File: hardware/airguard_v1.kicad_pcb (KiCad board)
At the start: 2 copper layers, 2 parts, among them U1 MH-Z19B, U2 ESP32_DEVKIT_C

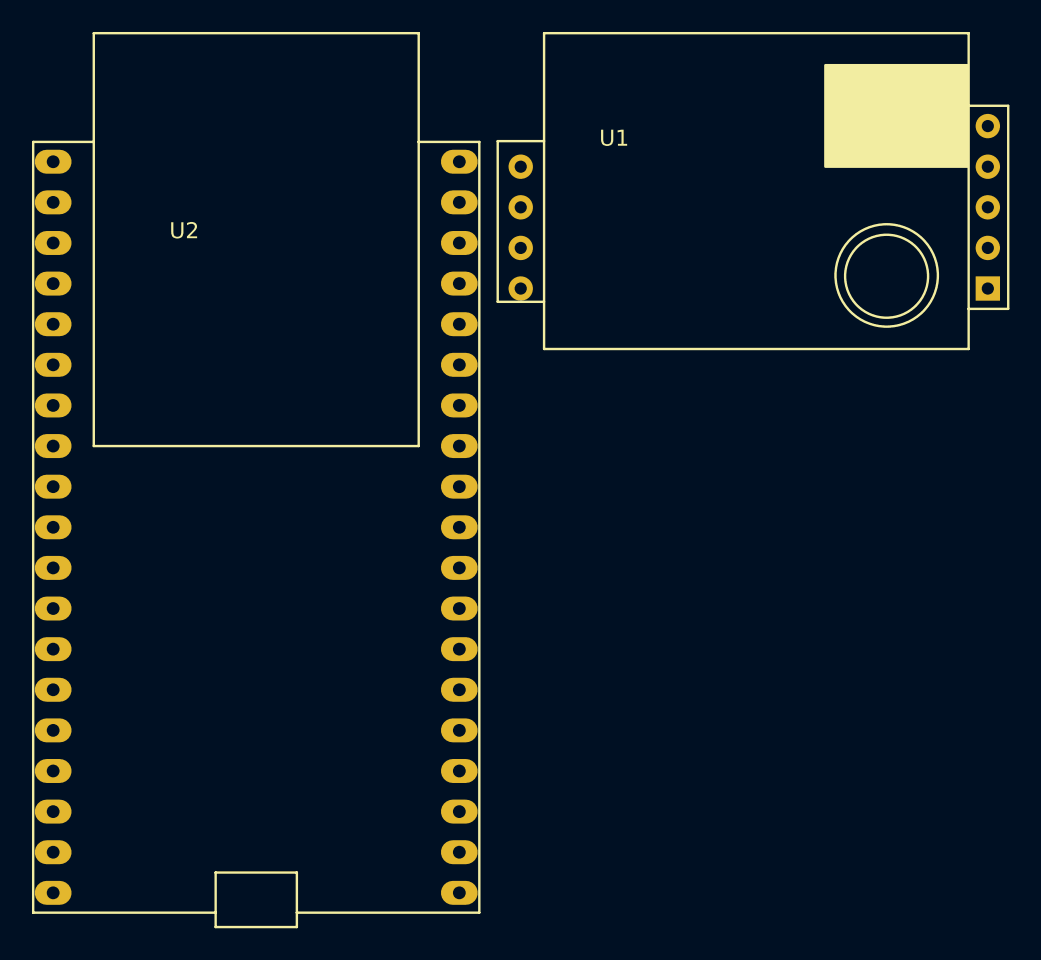
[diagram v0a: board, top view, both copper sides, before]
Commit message: Adding the OLED and all 3d models; connecting some of the signals to the corresponding ESP32 pins
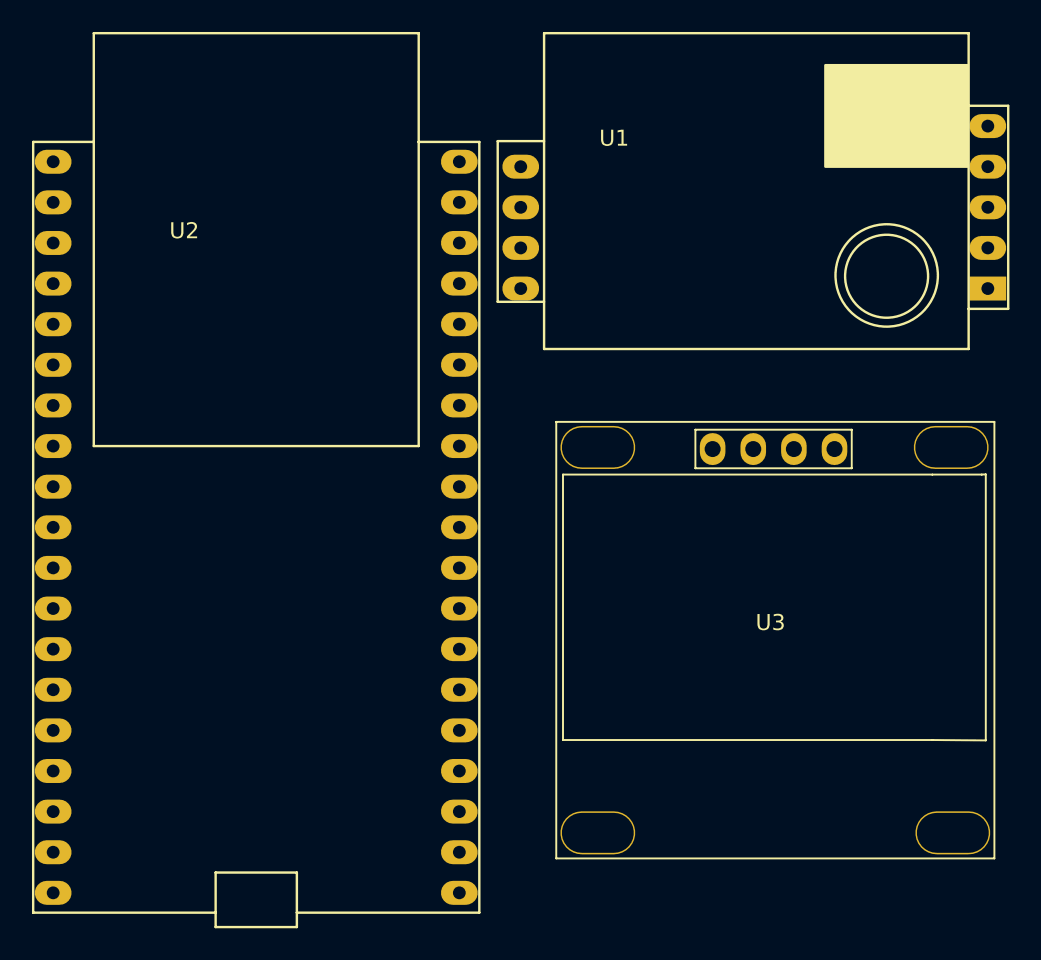
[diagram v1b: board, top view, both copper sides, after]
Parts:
- added U3: , footprints:SSD1306, F.Cu at (157.8, 109.3)
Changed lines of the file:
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@@
     (tracks 0)
     (zones 0)
-    (modules 2)
-    (nets 43)
+    (modules 3)
+    (nets 47)
   )
   (page A4)
@@
   (net 41 "Net-(U2-Pad2)")
   (net 42 +3V3)
+  (net 43 "Net-(U3-Pad4)")
+  (net 44 "Net-(U3-Pad3)")
+  (net 45 "Net-(U3-Pad1)")
+  (net 46 "Net-(U3-Pad2)")
   (net_class Default "This is the default net class."
     (clearance 0.2)
@@
     (add_net "Net-(U2-Pad8)")
     (add_net "Net-(U2-Pad9)")
+    (add_net "Net-(U3-Pad1)")
+    (add_net "Net-(U3-Pad2)")
+    (add_net "Net-(U3-Pad3)")
+    (add_net "Net-(U3-Pad4)")
+  )
+  (module footprints:SSD1306 (layer F.Cu)
+    (at 157.7975 109.347)
+    (fp_text reference U3 (at 0 0.254) (layer F.SilkS)
+      (effects (font (size 1 1) (thickness 0.15)))
+    )
+    (fp_text value "" (at 0 0) (layer F.SilkS)
+      (effects (font (size 1.27 1.27) (thickness 0.15)))
+    )
+    (fp_line (start 13.462 -9.017) (end 13.208 -9.005) (layer F.SilkS) (width 0.12))
+    (fp_line (start 13.462 7.62) (end 13.462 -9.017) (layer F.SilkS) (width 0.12))
+    (fp_line (start 10.122 7.595) (end 13.462 7.62) (layer F.SilkS) (width 0.12))
+    (fp_line (start 10.122 -9.005) (end 13.208 -9.005) (layer F.SilkS) (width 0.12))
+    (fp_line (start -4.699 -11.811) (end -4.699 -9.398) (layer F.SilkS) (width 0.12))
+    (fp_line (start 5.08 -9.398) (end -4.699 -9.398) (layer F.SilkS) (width 0.12))
+    (fp_line (start 5.08 -11.811) (end 5.08 -9.398) (layer F.SilkS) (width 0.12))
+    (fp_line (start -4.699 -11.811) (end 5.08 -11.811) (layer F.SilkS) (width 0.12))
+    (fp_line (start -12.978 -9.005) (end 10.122 -9.005) (layer F.SilkS) (width 0.12))
+    (fp_line (start -12.978 7.595) (end -12.978 -9.005) (layer F.SilkS) (width 0.12))
+    (fp_line (start 10.122 7.595) (end -12.978 7.595) (layer F.SilkS) (width 0.12))
+    (fp_line (start -13.4 15) (end -13.4 -12.3) (layer F.SilkS) (width 0.12))
+    (fp_line (start 14 15) (end -13.4 15) (layer F.SilkS) (width 0.12))
+    (fp_line (start 14 -12.3) (end 14 15) (layer F.SilkS) (width 0.12))
+    (fp_line (start -13.4 -12.3) (end 14 -12.3) (layer F.SilkS) (width 0.12))
+    (pad "" thru_hole oval (at -10.8 13.4 180) (size 4.68 2.69) (drill oval 4.5 2.5) (layers *.Cu *.Mask))
+    (pad "" thru_hole oval (at 11.4 13.4 180) (size 4.68 2.69) (drill oval 4.5 2.5) (layers *.Cu *.Mask))
+    (pad "" thru_hole oval (at 11.3 -10.7 180) (size 4.68 2.69) (drill oval 4.5 2.5) (layers *.Cu *.Mask))
+    (pad "" thru_hole oval (at -10.8 -10.7 180) (size 4.68 2.69) (drill oval 4.5 2.5) (layers *.Cu *.Mask))
+    (pad 4 thru_hole oval (at 4 -10.6 90) (size 2 1.6) (drill 1) (layers *.Cu B.Mask)
+      (net 43 "Net-(U3-Pad4)"))
+    (pad 3 thru_hole oval (at 1.46 -10.6 90) (size 2 1.6) (drill 1) (layers *.Cu B.Mask)
+      (net 44 "Net-(U3-Pad3)"))
+    (pad 1 thru_hole oval (at -3.62 -10.6 90) (size 2 1.6) (drill 1) (layers *.Cu B.Mask)
+      (net 45 "Net-(U3-Pad1)"))
+    (pad 2 thru_hole oval (at -1.08 -10.6 90) (size 2 1.6) (drill 1) (layers *.Cu B.Mask)
+      (net 46 "Net-(U3-Pad2)"))
+    (model "${KIPRJMOD}/3d/OLED TFT 0.96 inch 64x128 monochrome.STEP"
+      (offset (xyz 0 12 2.5))
+      (scale (xyz 1 1 1))
+      (rotate (xyz -90 0 0))
+    )
+  )
+  (module footprints:Winsen_MH-Z19B (layer F.Cu)
+    (at 171.3865 74.7395)
+    (fp_text reference U1 (at -23.368 4.572) (layer F.SilkS)
+      (effects (font (size 1 1) (thickness 0.15)))
+    )
+    (fp_text value MH-Z19B (at -19.05 0.762) (layer F.Fab)
+      (effects (font (size 1 1) (thickness 0.15)))
+    )
+    (fp_line (start -1.2 -2) (end -1.2 17.75) (layer F.SilkS) (width 0.15))
+    (fp_poly (pts (xy -10.16 0) (xy -10.16 6.35) (xy -1.27 6.35) (xy -1.27 0)) (layer F.SilkS) (width 0.15))
+    (fp_circle (center -6.330656 13.2) (end -8.530656 11.825) (layer F.SilkS) (width 0.15))
+    (fp_circle (center -6.325 13.15) (end -9.425 12.35) (layer F.SilkS) (width 0.15))
+    (fp_line (start -27.75 17.75) (end -1.2 17.75) (layer F.SilkS) (width 0.15))
+    (fp_line (start -27.75 -2) (end -27.75 17.75) (layer F.SilkS) (width 0.15))
+    (fp_line (start -30.65 14.8) (end -27.75 14.8) (layer F.SilkS) (width 0.15))
+    (fp_line (start -30.65 4.75) (end -30.65 14.8) (layer F.SilkS) (width 0.15))
+    (fp_line (start -27.75 4.75) (end -30.65 4.75) (layer F.SilkS) (width 0.15))
+    (fp_line (start -1.27 2.54) (end 1.27 2.54) (layer F.SilkS) (width 0.15))
+    (fp_line (start 1.275 2.54) (end 1.275 15.24) (layer F.SilkS) (width 0.15))
+    (fp_line (start 1.27 15.24) (end -1.205 15.24) (layer F.SilkS) (width 0.15))
+    (fp_line (start -1.2 -2) (end -27.75 -2) (layer F.SilkS) (width 0.15))
+    (pad 1 thru_hole rect (at 0 13.97) (size 2.3 1.5) (drill 0.8) (layers *.Cu B.Mask)
+      (net 1 "Net-(U1-Pad1)"))
+    (pad 2 thru_hole oval (at 0 11.43) (size 2.3 1.5) (drill 0.8) (layers *.Cu B.Mask)
+      (net 2 "Net-(U1-Pad2)"))
+    (pad 3 thru_hole oval (at 0 8.89) (size 2.3 1.5) (drill 0.8) (layers *.Cu B.Mask)
+      (net 3 "Net-(U1-Pad3)"))
+    (pad 4 thru_hole oval (at 0 6.35) (size 2.3 1.5) (drill 0.8) (layers *.Cu B.Mask)
+      (net 4 "Net-(U1-Pad4)"))
+    (pad 5 thru_hole oval (at 0 3.81) (size 2.3 1.5) (drill 0.8) (layers *.Cu B.Mask)
+      (net 5 "Net-(U1-Pad5)"))
+    (pad 6 thru_hole oval (at -29.21 13.97) (size 2.3 1.5) (drill 0.8) (layers *.Cu B.Mask)
+      (net 6 +5V))
+    (pad 7 thru_hole oval (at -29.21 11.43) (size 2.3 1.5) (drill 0.8) (layers *.Cu B.Mask)
+      (net 7 GND))
+    (pad 8 thru_hole oval (at -29.21 8.89) (size 2.3 1.5) (drill 0.8) (layers *.Cu B.Mask)
+      (net 8 "Net-(U1-Pad8)"))
+    (pad 9 thru_hole oval (at -29.21 6.35) (size 2.3 1.5) (drill 0.8) (layers *.Cu B.Mask)
+      (net 9 "Net-(U1-Pad9)"))
+    (model ${KIPRJMOD}/3d/MH-Z19C.STEP
+      (offset (xyz 81.5 -74 3))
+      (scale (xyz 1 1 1))
+      (rotate (xyz 90 180 90))
+    )
   )
   (module footprints:ESP32_DEVKIT_C (layer F.Cu)
@@
     (pad 1 thru_hole oval (at -12.7 -22.86) (size 2.3 1.5) (drill 0.8) (layers *.Cu B.Mask)
       (net 42 +3V3))
-  )
-  (module footprints:Winsen_MH-Z19B (layer F.Cu)
-    (at 171.3865 74.7395)
-    (fp_text reference U1 (at -23.368 4.572) (layer F.SilkS)
-      (effects (font (size 1 1) (thickness 0.15)))
-    )
-    (fp_text value MH-Z19B (at -19.05 0.762) (layer F.Fab)
-      (effects (font (size 1 1) (thickness 0.15)))
-    )
-    (fp_line (start -1.2 -2) (end -1.2 17.75) (layer F.SilkS) (width 0.15))
-    (fp_poly (pts (xy -10.16 0) (xy -10.16 6.35) (xy -1.27 6.35) (xy -1.27 0)) (layer F.SilkS) (width 0.15))
-    (fp_circle (center -6.330656 13.2) (end -8.530656 11.825) (layer F.SilkS) (width 0.15))
-    (fp_circle (center -6.325 13.15) (end -9.425 12.35) (layer F.SilkS) (width 0.15))
-    (fp_line (start -27.75 17.75) (end -1.2 17.75) (layer F.SilkS) (width 0.15))
-    (fp_line (start -27.75 -2) (end -27.75 17.75) (layer F.SilkS) (width 0.15))
-    (fp_line (start -30.65 14.8) (end -27.75 14.8) (layer F.SilkS) (width 0.15))
-    (fp_line (start -30.65 4.75) (end -30.65 14.8) (layer F.SilkS) (width 0.15))
-    (fp_line (start -27.75 4.75) (end -30.65 4.75) (layer F.SilkS) (width 0.15))
-    (fp_line (start -1.27 2.54) (end 1.27 2.54) (layer F.SilkS) (width 0.15))
-    (fp_line (start 1.275 2.54) (end 1.275 15.24) (layer F.SilkS) (width 0.15))
-    (fp_line (start 1.27 15.24) (end -1.205 15.24) (layer F.SilkS) (width 0.15))
-    (fp_line (start -1.2 -2) (end -27.75 -2) (layer F.SilkS) (width 0.15))
-    (pad 1 thru_hole rect (at 0 13.97) (size 1.524 1.524) (drill 0.762) (layers *.Cu *.Mask)
-      (net 1 "Net-(U1-Pad1)"))
-    (pad 2 thru_hole circle (at 0 11.43) (size 1.524 1.524) (drill 0.762) (layers *.Cu *.Mask)
-      (net 2 "Net-(U1-Pad2)"))
-    (pad 3 thru_hole circle (at 0 8.89) (size 1.524 1.524) (drill 0.762) (layers *.Cu *.Mask)
-      (net 3 "Net-(U1-Pad3)"))
-    (pad 4 thru_hole circle (at 0 6.35) (size 1.524 1.524) (drill 0.762) (layers *.Cu *.Mask)
-      (net 4 "Net-(U1-Pad4)"))
-    (pad 5 thru_hole circle (at 0 3.81) (size 1.524 1.524) (drill 0.762) (layers *.Cu *.Mask)
-      (net 5 "Net-(U1-Pad5)"))
-    (pad 6 thru_hole circle (at -29.21 13.97) (size 1.524 1.524) (drill 0.762) (layers *.Cu *.Mask)
-      (net 6 +5V))
-    (pad 7 thru_hole circle (at -29.21 11.43) (size 1.524 1.524) (drill 0.762) (layers *.Cu *.Mask)
-      (net 7 GND))
-    (pad 8 thru_hole circle (at -29.21 8.89) (size 1.524 1.524) (drill 0.762) (layers *.Cu *.Mask)
-      (net 8 "Net-(U1-Pad8)"))
-    (pad 9 thru_hole circle (at -29.21 6.35) (size 1.524 1.524) (drill 0.762) (layers *.Cu *.Mask)
-      (net 9 "Net-(U1-Pad9)"))
+    (model ${KIPRJMOD}/3d/ESP32-WROOM-32D-Assembly.STEP
+      (offset (xyz 0 0 2.5))
+      (scale (xyz 1 1 1))
+      (rotate (xyz -90 0 0))
+    )
   )
 )
